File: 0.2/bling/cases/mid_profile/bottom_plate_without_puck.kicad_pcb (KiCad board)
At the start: 2 copper layers, 110.3 x 98 mm, 0 parts

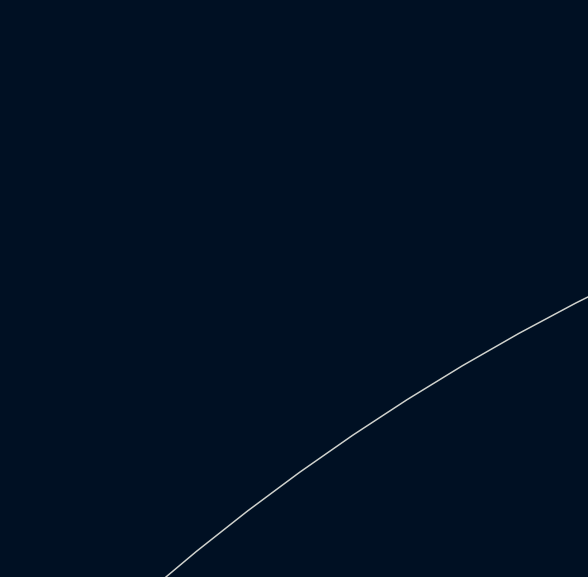
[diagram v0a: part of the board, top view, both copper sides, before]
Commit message: Add dummy component to each plate case
This works around a segfault in Pcbdraw which prevents renders in the
edge case where a PCB file has no module.
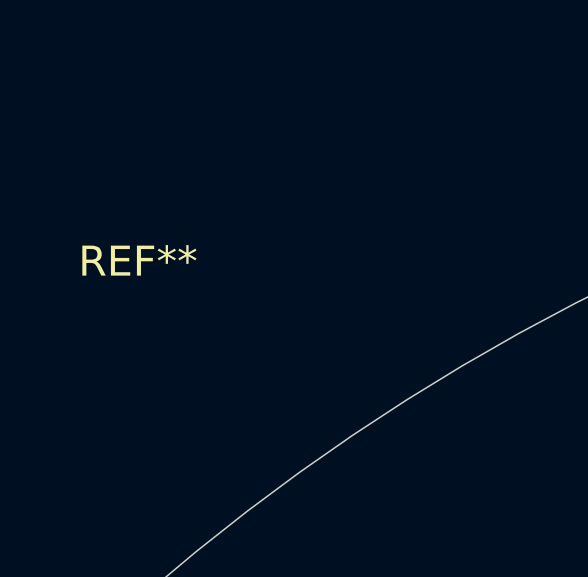
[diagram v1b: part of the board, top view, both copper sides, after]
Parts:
- added REF**: dummy, dummy:dummy, F.Cu at (12.1, 12.3)
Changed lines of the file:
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@@
     (tracks 0)
     (zones 0)
-    (modules 0)
+    (modules 1)
     (nets 1)
   )
@@
     (uvia_drill 0.1)
   )
+  (module dummy:dummy (layer F.Cu)
+    (at 12.1 12.3)
+    (fp_text reference REF** (at 0 0.5) (layer F.SilkS)
+      (effects (font (size 1 1) (thickness 0.15)))
+    )
+    (fp_text value dummy (at 0 -0.5) (layer F.Fab)
+      (effects (font (size 1 1) (thickness 0.15)))
+    )
+  )
   (gr_arc (start 61.59 173.76) (end 105.638 99.588735) (angle -15.4) (layer Cmts.User) (width 0.05))
